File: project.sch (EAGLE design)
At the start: 12 parts, among them IC1 board outline, U1 INA169, U2 TPS22958

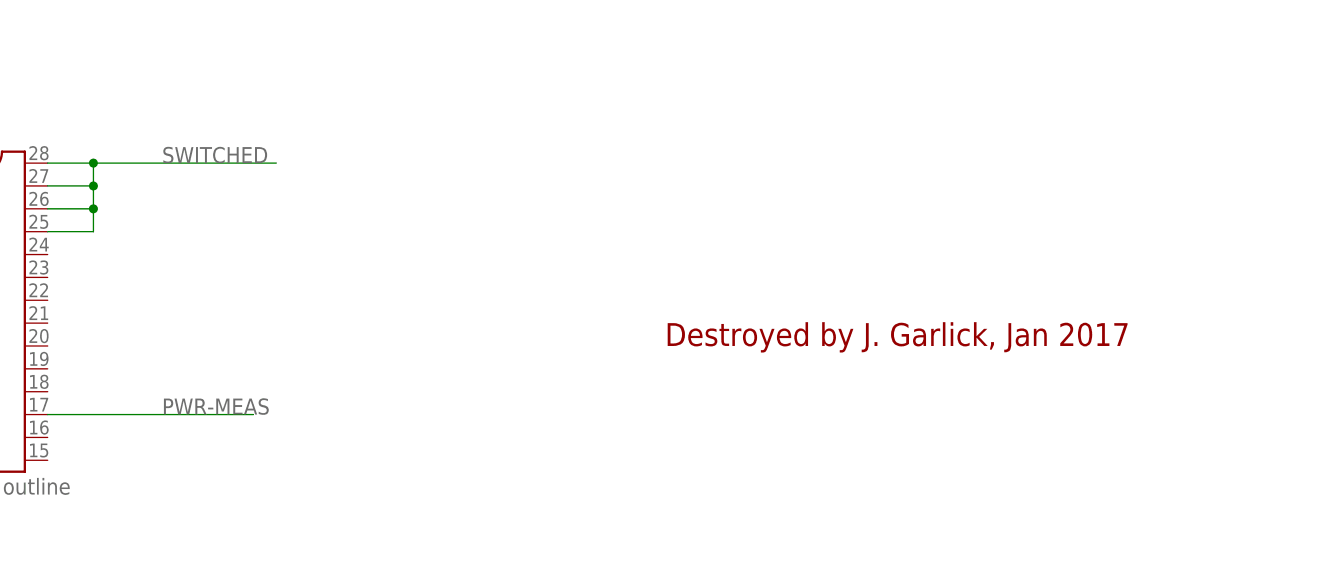
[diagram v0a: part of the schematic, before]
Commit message: project.sch: replace frame with generic one
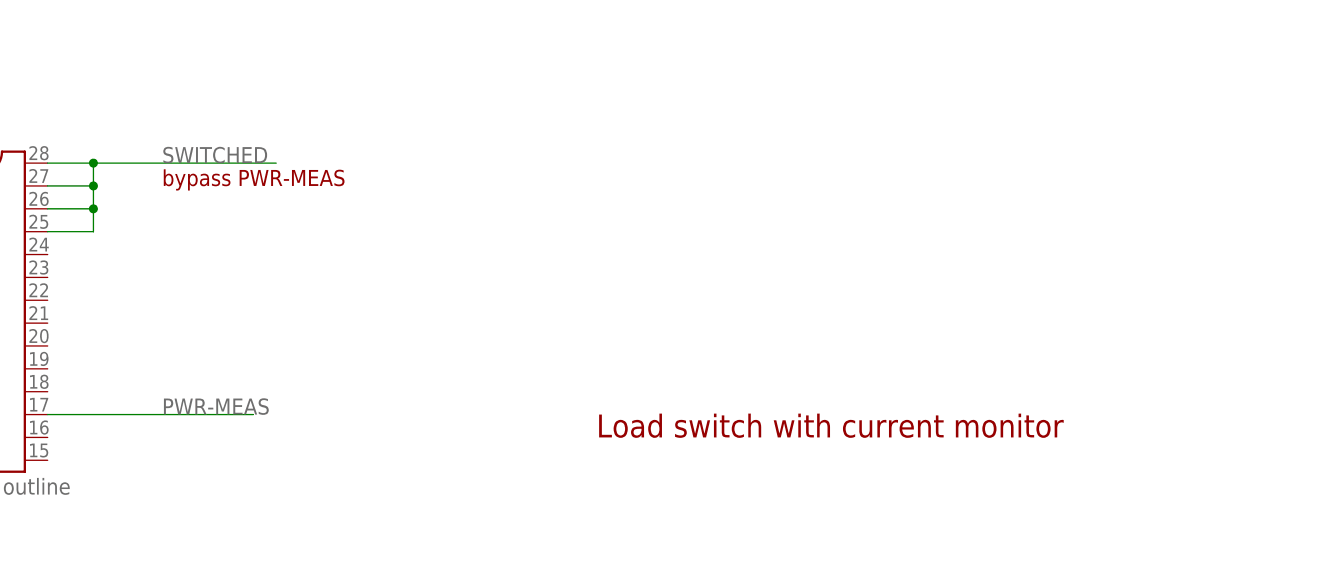
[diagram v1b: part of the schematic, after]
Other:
- note added: "Load switch with current monitor"
- note added: "bypass PWR-MEAS"
- note removed: "Destroyed by J. Garlick, Jan 2017"
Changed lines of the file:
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@@
 <grid distance="0.1" unitdist="inch" unit="inch" style="lines" multiple="1" display="no" altdistance="0.01" altunitdist="inch" altunit="inch"/>
 <layers>
-<layer number="1" name="Top" color="4" fill="1" visible="yes" active="no"/>
-<layer number="2" name="Route2" color="1" fill="3" visible="yes" active="no"/>
-<layer number="3" name="Route3" color="4" fill="3" visible="yes" active="no"/>
-<layer number="4" name="Route4" color="1" fill="4" visible="yes" active="no"/>
-<layer number="5" name="Route5" color="4" fill="4" visible="yes" active="no"/>
-<layer number="6" name="Route6" color="1" fill="8" visible="yes" active="no"/>
-<layer number="7" name="Route7" color="4" fill="8" visible="yes" active="no"/>
-<layer number="8" name="Route8" color="1" fill="2" visible="yes" active="no"/>
-<layer number="9" name="Route9" color="4" fill="2" visible="yes" active="no"/>
-<layer number="10" name="Route10" color="1" fill="7" visible="yes" active="no"/>
-<layer number="11" name="Route11" color="4" fill="7" visible="yes" active="no"/>
-<layer number="12" name="Route12" color="1" fill="5" visible="yes" active="no"/>
-<layer number="13" name="Route13" color="4" fill="5" visible="yes" active="no"/>
-<layer number="14" name="Route14" color="1" fill="6" visible="yes" active="no"/>
-<layer number="15" name="Route15" color="4" fill="6" visible="yes" active="no"/>
-<layer number="16" name="Bottom" color="1" fill="1" visible="yes" active="no"/>
-<layer number="17" name="Pads" color="2" fill="1" visible="yes" active="no"/>
-<layer number="18" name="Vias" color="2" fill="1" visible="yes" active="no"/>
-<layer number="19" name="Unrouted" color="6" fill="1" visible="yes" active="no"/>
-<layer number="20" name="Dimension" color="15" fill="1" visible="yes" active="no"/>
-<layer number="21" name="tPlace" color="14" fill="1" visible="yes" active="no"/>
-<layer number="22" name="bPlace" color="11" fill="1" visible="yes" active="no"/>
-<layer number="23" name="tOrigins" color="15" fill="1" visible="yes" active="no"/>
-<layer number="24" name="bOrigins" color="15" fill="1" visible="yes" active="no"/>
-<layer number="25" name="tNames" color="7" fill="1" visible="yes" active="no"/>
-<layer number="26" name="bNames" color="7" fill="1" visible="yes" active="no"/>
-<layer number="27" name="tValues" color="7" fill="1" visible="yes" active="no"/>
-<layer number="28" name="bValues" color="7" fill="1" visible="yes" active="no"/>
+<layer number="1" name="Top" color="4" fill="1" visible="no" active="no"/>
+<layer number="2" name="Route2" color="1" fill="3" visible="no" active="no"/>
+<layer number="3" name="Route3" color="4" fill="3" visible="no" active="no"/>
+<layer number="4" name="Route4" color="1" fill="4" visible="no" active="no"/>
+<layer number="5" name="Route5" color="4" fill="4" visible="no" active="no"/>
+<layer number="6" name="Route6" color="1" fill="8" visible="no" active="no"/>
+<layer number="7" name="Route7" color="4" fill="8" visible="no" active="no"/>
+<layer number="8" name="Route8" color="1" fill="2" visible="no" active="no"/>
+<layer number="9" name="Route9" color="4" fill="2" visible="no" active="no"/>
+<layer number="10" name="Route10" color="1" fill="7" visible="no" active="no"/>
+<layer number="11" name="Route11" color="4" fill="7" visible="no" active="no"/>
+<layer number="12" name="Route12" color="1" fill="5" visible="no" active="no"/>
+<layer number="13" name="Route13" color="4" fill="5" visible="no" active="no"/>
+<layer number="14" name="Route14" color="1" fill="6" visible="no" active="no"/>
+<layer number="15" name="Route15" color="4" fill="6" visible="no" active="no"/>
+<layer number="16" name="Bottom" color="1" fill="1" visible="no" active="no"/>
+<layer number="17" name="Pads" color="2" fill="1" visible="no" active="no"/>
+<layer number="18" name="Vias" color="2" fill="1" visible="no" active="no"/>
+<layer number="19" name="Unrouted" color="6" fill="1" visible="no" active="no"/>
+<layer number="20" name="Dimension" color="15" fill="1" visible="no" active="no"/>
+<layer number="21" name="tPlace" color="14" fill="1" visible="no" active="no"/>
+<layer number="22" name="bPlace" color="11" fill="1" visible="no" active="no"/>
+<layer number="23" name="tOrigins" color="15" fill="1" visible="no" active="no"/>
+<layer number="24" name="bOrigins" color="15" fill="1" visible="no" active="no"/>
+<layer number="25" name="tNames" color="7" fill="1" visible="no" active="no"/>
+<layer number="26" name="bNames" color="7" fill="1" visible="no" active="no"/>
+<layer number="27" name="tValues" color="7" fill="1" visible="no" active="no"/>
+<layer number="28" name="bValues" color="7" fill="1" visible="no" active="no"/>
 <layer number="29" name="tStop" color="7" fill="3" visible="no" active="no"/>
 <layer number="30" name="bStop" color="7" fill="6" visible="no" active="no"/>
@@
 <layer number="35" name="tGlue" color="7" fill="4" visible="no" active="no"/>
 <layer number="36" name="bGlue" color="7" fill="5" visible="no" active="no"/>
-<layer number="37" name="tTest" color="7" fill="1" visible="yes" active="no"/>
-<layer number="38" name="bTest" color="7" fill="1" visible="yes" active="no"/>
+<layer number="37" name="tTest" color="7" fill="1" visible="no" active="no"/>
+<layer number="38" name="bTest" color="7" fill="1" visible="no" active="no"/>
 <layer number="39" name="tKeepout" color="4" fill="11" visible="no" active="no"/>
 <layer number="40" name="bKeepout" color="1" fill="11" visible="no" active="no"/>
@@
 <layer number="44" name="Drills" color="7" fill="1" visible="no" active="no"/>
 <layer number="45" name="Holes" color="7" fill="1" visible="no" active="no"/>
-<layer number="46" name="Milling" color="3" fill="1" visible="yes" active="no"/>
-<layer number="47" name="Measures" color="7" fill="1" visible="yes" active="no"/>
-<layer number="48" name="Document" color="7" fill="1" visible="yes" active="no"/>
-<layer number="49" name="Reference" color="7" fill="1" visible="yes" active="no"/>
-<layer number="50" name="dxf" color="7" fill="1" visible="yes" active="no"/>
-<layer number="51" name="tDocu" color="7" fill="1" visible="yes" active="no"/>
-<layer number="52" name="bDocu" color="7" fill="1" visible="yes" active="no"/>
-<layer number="53" name="tGND_GNDA" color="7" fill="9" visible="yes" active="no"/>
-<layer number="54" name="bGND_GNDA" color="1" fill="9" visible="yes" active="no"/>
-<layer number="56" name="wert" color="7" fill="1" visible="yes" active="no"/>
-<layer number="57" name="tCAD" color="7" fill="1" visible="yes" active="no"/>
+<layer number="46" name="Milling" color="3" fill="1" visible="no" active="no"/>
+<layer number="47" name="Measures" color="7" fill="1" visible="no" active="no"/>
+<layer number="48" name="Document" color="7" fill="1" visible="no" active="no"/>
+<layer number="49" name="Reference" color="7" fill="1" visible="no" active="no"/>
+<layer number="50" name="dxf" color="7" fill="1" visible="no" active="no"/>
+<layer number="51" name="tDocu" color="7" fill="1" visible="no" active="no"/>
+<layer number="52" name="bDocu" color="7" fill="1" visible="no" active="no"/>
+<layer number="53" name="tGND_GNDA" color="7" fill="9" visible="no" active="no"/>
+<layer number="54" name="bGND_GNDA" color="1" fill="9" visible="no" active="no"/>
+<layer number="56" name="wert" color="7" fill="1" visible="no" active="no"/>
+<layer number="57" name="tCAD" color="7" fill="1" visible="no" active="no"/>
 <layer number="90" name="Modules" color="5" fill="1" visible="yes" active="yes"/>
 <layer number="91" name="Nets" color="2" fill="1" visible="yes" active="yes"/>
@@
 </classes>
 <parts>
-<part name="U$1" library="microbuilder" deviceset="FRAME_A4_ADAFRUIT" device=""/>
 <part name="U$4" library="microbuilder" deviceset="GND" device=""/>
 <part name="P+3" library="microbuilder" deviceset="VCC" device=""/>
@@
 <part name="P+2" library="microbuilder" deviceset="VCC" device=""/>
 <part name="U$6" library="microbuilder" deviceset="GND" device=""/>
+<part name="FRAME1" library="frames" deviceset="FRAME_A_L" device=""/>
 </parts>
 <sheets>
@@
 <text x="121.92" y="165.1" size="1.778" layer="94">PWR-MEAS = Iload * Rload * Rshunt / 1000</text>
 <text x="121.92" y="160.02" size="1.778" layer="94">PWR-MEAS = 1Volt per1 Amp</text>
-<text x="172.72" y="38.1" size="2.54" layer="94">Destroyed by J. Garlick, Jan 2017</text>
+<text x="165.1" y="27.94" size="2.54" layer="94">Load switch with current monitor</text>
+<text x="116.84" y="55.88" size="1.778" layer="94">bypass PWR-MEAS</text>
 </plain>
 <instances>
-<instance part="U$1" gate="G$1" x="0" y="0"/>
 <instance part="U$4" gate="G$1" x="152.4" y="91.44"/>
 <instance part="P+3" gate="VCC" x="142.24" y="147.32"/>
@@
 <instance part="P+2" gate="VCC" x="50.8" y="38.1"/>
 <instance part="U$6" gate="G$1" x="86.36" y="17.78"/>
+<instance part="FRAME1" gate="G$1" x="-10.16" y="0"/>
+<instance part="FRAME1" gate="G$2" x="162.56" y="0"/>
 </instances>
 <busses>
